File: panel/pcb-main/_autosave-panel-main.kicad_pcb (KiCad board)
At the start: 2 copper layers, 191.7 x 104.9 mm, 97 parts, among them J1 PSU IN, J2 SPEED CTRL, J3 ICSP, J4 PUSH-BUTTON, J5 DISPLAY, J6 CONN-L1, J7 CONN-L2, J8 CONN-R1, J9 CONN-R2, K1 TRK2233-12DC, K10 TRK2233-12DC, K11 TRK2233-12DC, K2 TRK2233-12DC, K3 TRK2233-12DC, K4 TRK2233-12DC, K5 TRK2233-12DC, K6 TRK2233-12DC, K7 TRK2233-12DC, K8 TRK2233-12DC, K9 TRK2233-12DC, Q1 2N2222, Q10 BD679, Q11 BD679, Q12 BD679, Q13 BD679, Q14 2N2222, Q15 BD679, Q16 BD679, Q17 BD679, Q18 BD679, Q19 BD679, Q2 TIP32, Q3 BD679, Q37 BD679, Q4 BD679, Q5 BD679, Q6 BD679, Q7 BD679, Q8 BD679, Q9 TIP32, U1 LM7805_TO220, U2 74HC595, U3 74HC595, U4 74HC595, U5 74HC595, U6 ULN2003A, U7 ULN2003A, Y1 20MHz

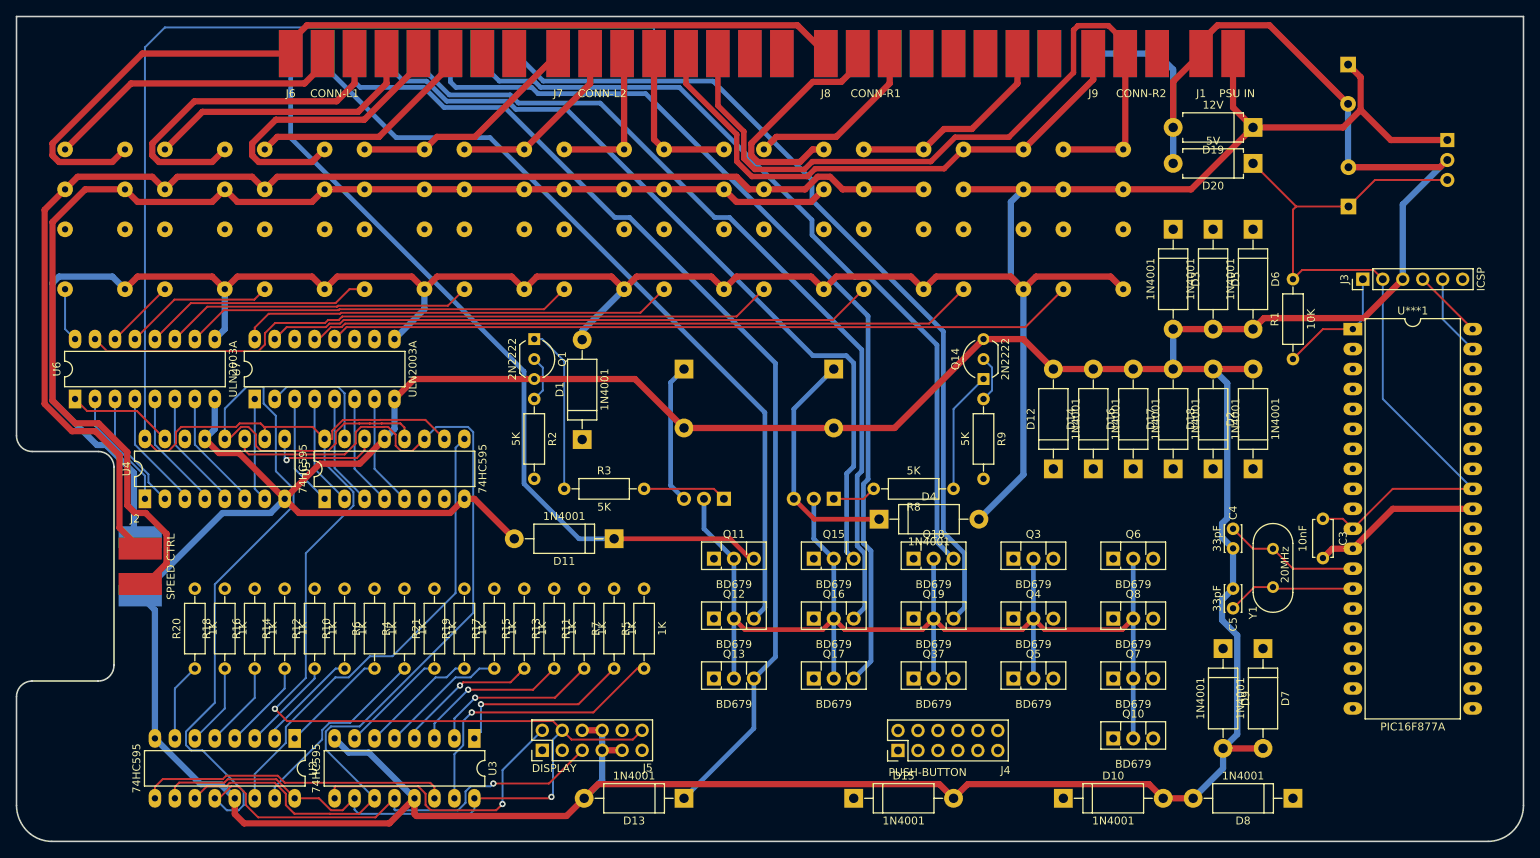
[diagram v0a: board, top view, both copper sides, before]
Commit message: PCB Updates and added panel-fw project.
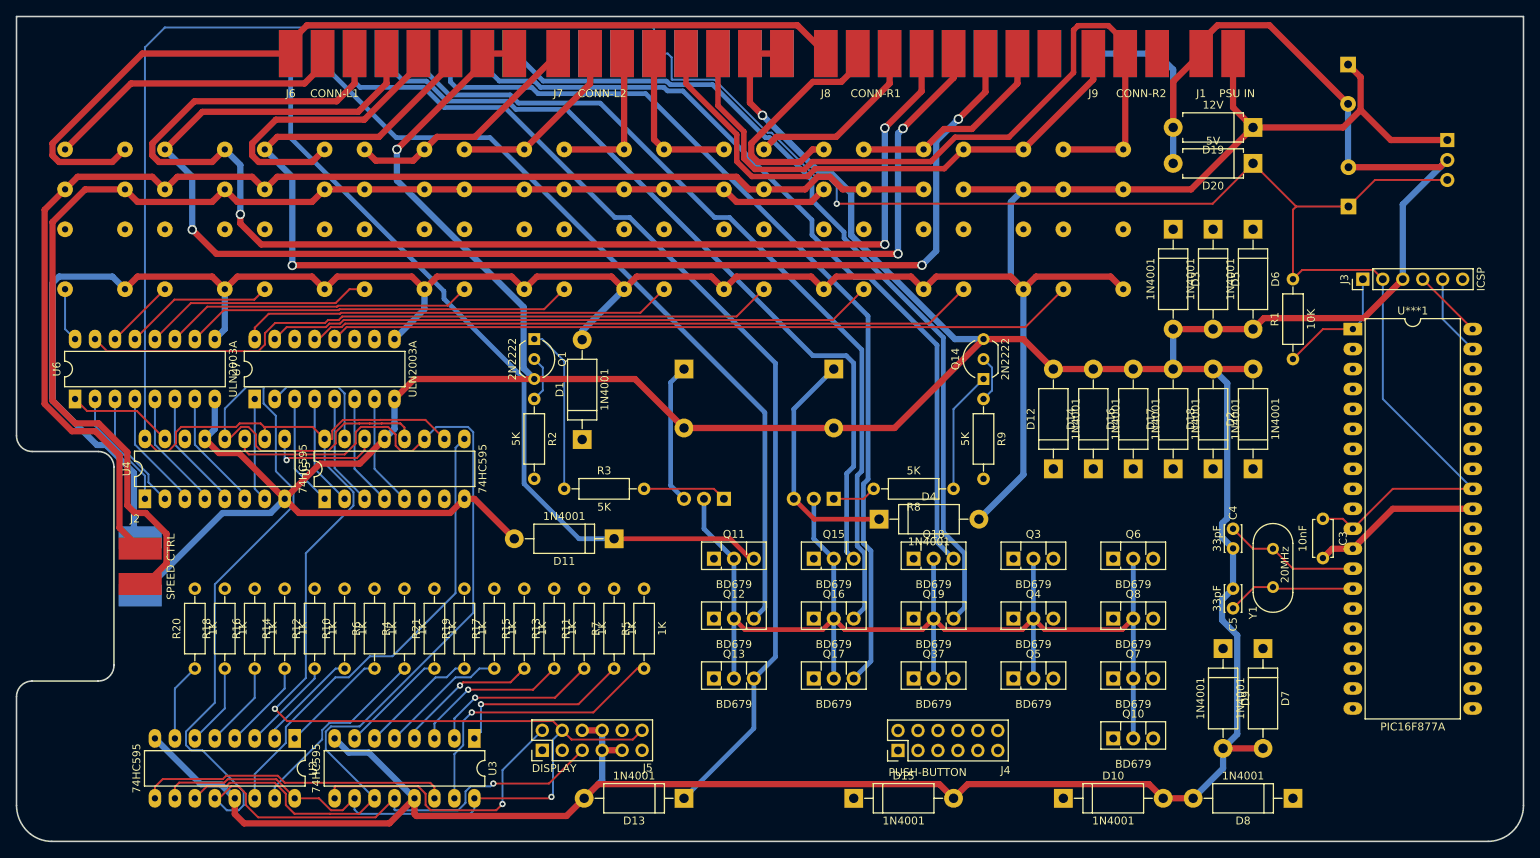
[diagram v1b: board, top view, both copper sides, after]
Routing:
- net /Feed Relays/FEED[C-]: track 35.5 -> 166.6 mm, vias 0 -> 3
- net /Feed Relays/FEED[D-]: track 29.6 -> 156.2 mm, vias 0 -> 3
- net /Feed Relays/FEED[C+]: track 44.5 -> 164.0 mm, vias 0 -> 3
- net GND: track 628.9 -> 722.8 mm, vias 0 -> 2
- net +5V: track 421.5 -> 510.6 mm, vias 2 -> 3
- net /Feed Relays/FEED[E+]: track 29.7 -> 30.9 mm
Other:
- net class Aux Feeds: via_dia 0.8 -> 1.2; via_drill 0.4 -> 0.8
- net class Points Coils: via_dia 0.8 -> 1.2; via_drill 0.4 -> 0.8
- net class Power: via_dia 0.8 -> 1.2; via_drill 0.4 -> 0.8
- net class Track Feeds: via_dia 1 -> 1.2
